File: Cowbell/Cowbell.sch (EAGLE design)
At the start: 70 parts, among them IC1 LM741P, Q1 2N3906, T1 2N3904, T2 2N3904, T3 2N3904, T4 2N3904, T5 2N3904, T6 2N3904, T7 2N3904, T8 2N3904

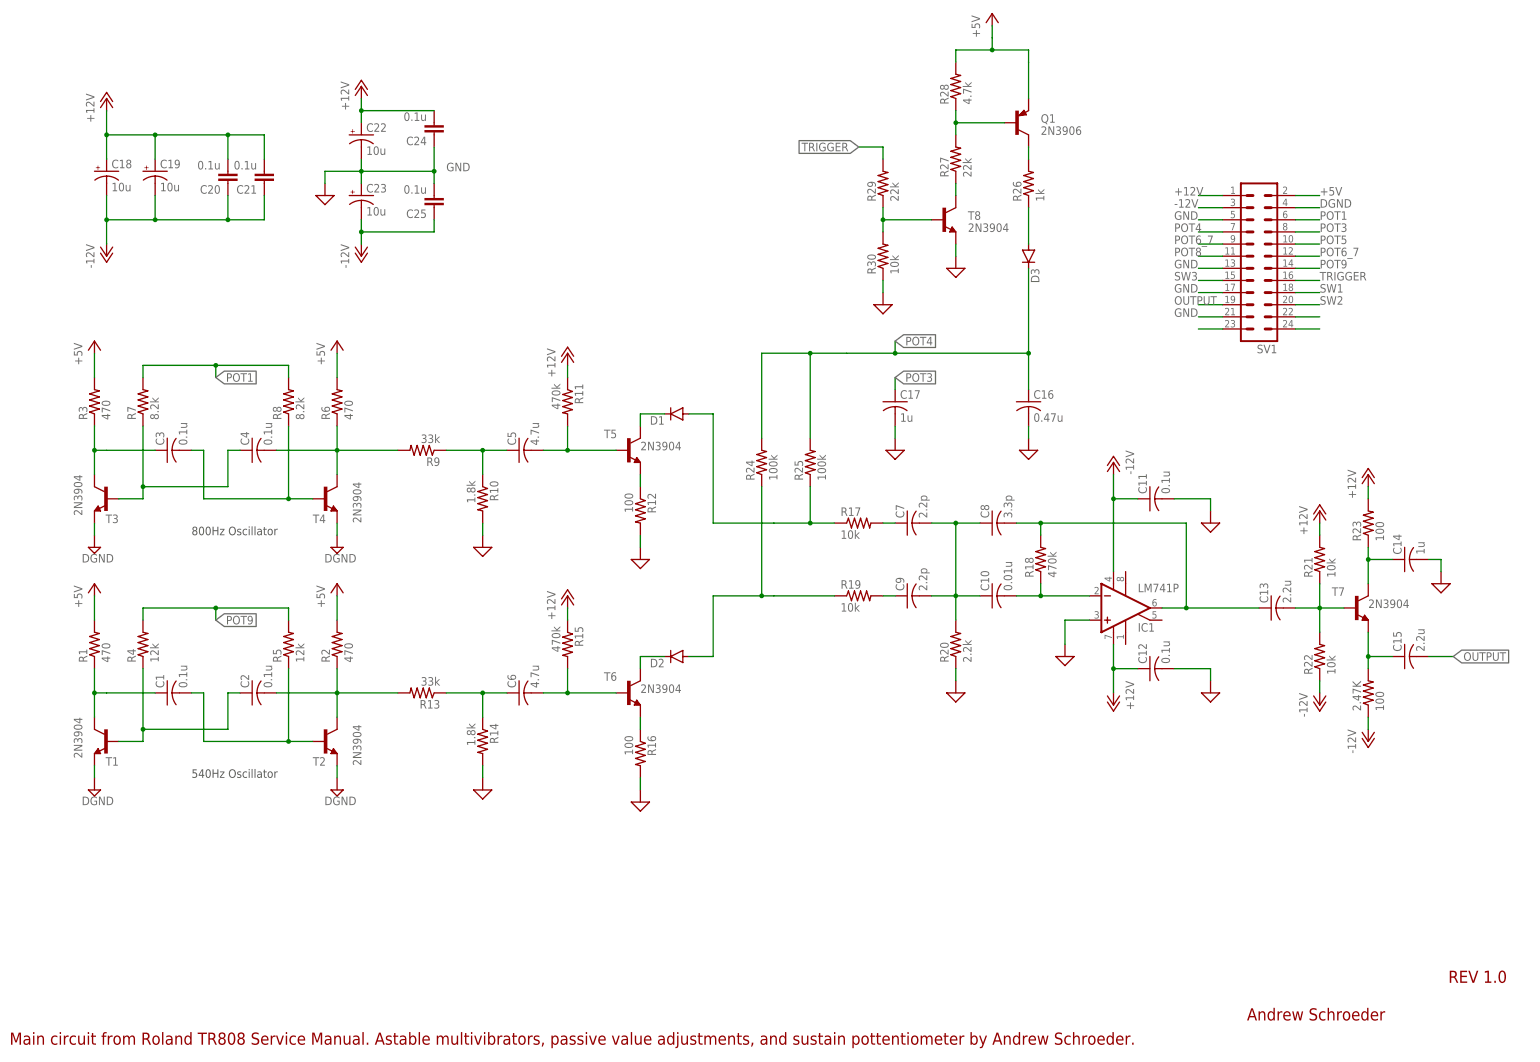
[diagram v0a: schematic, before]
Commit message: Placed parts on .brd file. Have to route yet.
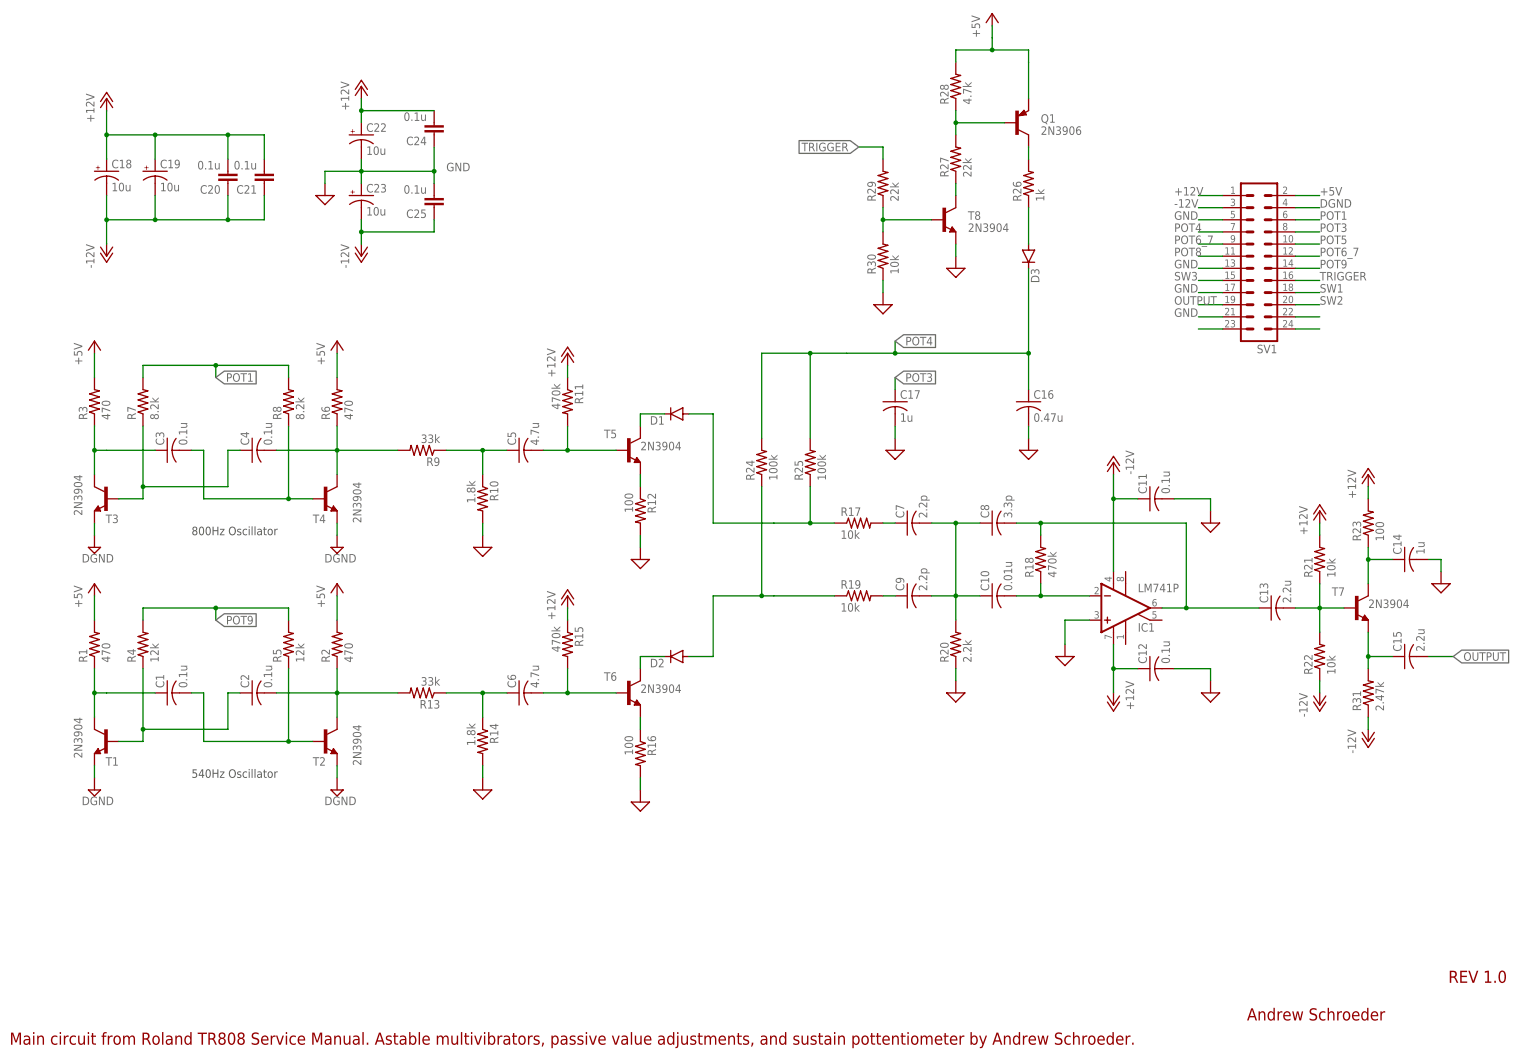
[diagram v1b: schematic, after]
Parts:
- R31: value 100 -> 2.47k
- renumbered 2.47K to R31
